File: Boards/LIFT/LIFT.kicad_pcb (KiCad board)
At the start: 4 copper layers, 58 x 82.5 mm, 11 parts, among them J1 Screw_Terminal_01x02, J2 393570004, J3 393570004, J4 393570004, J5 Screw_Terminal_01x02, U3 MAX485_MODULE_5V_LOGIC_TLL_TO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

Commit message: PCB Loadcells
Agora sim acho que ta acabado
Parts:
- added G***: LOGO, FEUP-text:Feup-text, B.Cu at (158.0, 144.5)
- added U6: ~, DCDCModule:DCDC_Module, F.Cu at (155.0, 137.9)
- U2: moved to B.Cu
- moved U2 22.2 mm to (134.4, 136.3), turned to 90 degrees
- moved J1 7.79 mm to (174.5, 138.8)
- moved A1 0.11 mm to (176.8, 88.7)
- moved U3 0.11 mm to (146.1, 116.2)
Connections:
- J1 pad 2: /3V3 -> /V_In
- J3 pad 3: /A1+ -> /A1-
- J3 pad 4: /A1- -> /A1+
- J4 pad 3: /A3+ -> /A3-
- J4 pad 4: /A3- -> /A3+
- U1 pad 3: /A3+ -> /A3-
- U1 pad 4: /A3- -> /A3+
- U4 pad 3: /A1+ -> /A1-
- U4 pad 4: /A1- -> /A1+
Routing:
- net /5V: track 92.6 -> 164.9 mm, vias 0 -> 1
- net GND: track 0.00 -> 51.3 mm
- net /SD_CLK: track 44.7 -> 61.2 mm
- net /SD_MOSI: track 43.2 -> 56.4 mm
- net /SD_CS: track 43.7 -> 56.8 mm
- net /V_In: track 0.00 -> 9.90 mm
- net /SD_MISO: track 59.8 -> 68.3 mm
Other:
- board size 58 x 82.5 mm -> 59 x 100 mm
- board text added: "Green White Black Red"
- board text added: "LIFT"
- board text added: "RS+ RS-"

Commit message: PCB LOADCELLS
PCB LOADCELLS
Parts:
- U2: moved to F.Cu
- moved U2 11.6 mm to (122.8, 136.4)
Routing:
- net GND: track 51.3 -> 34.1 mm
- net /SD_CS: track 56.8 -> 54.2 mm
- net /SD_MISO: track 68.3 -> 66.7 mm
- net /SD_MOSI: track 56.4 -> 54.9 mm
- net /SD_CLK: track 61.2 -> 59.8 mm

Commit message: PCB Lift Final
PCB Lift Final
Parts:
- moved G*** 3.01 mm to (155.0, 144.2)
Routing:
- net GND: track 34.1 -> 11.6 mm
- net /5V: track 164.9 -> 166.2 mm, vias 1 -> 0
- net /V_In: track 9.90 -> 11.1 mm
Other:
- board text added: "LEAVE SPACE FOR SD CARD"

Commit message: LIFT Finish
LIFT pcb finish
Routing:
- added copper zone on B.Cu, net /3V3
- added copper zone on F.Cu, net GND
- removed copper zone on In2.Cu, net /3V3
- removed copper zone on In1.Cu, net GND
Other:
- copper layers 4 -> 2

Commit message: LIFT PCB
LIFT PCB
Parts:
- added H1: MountingHole, MountingHole:MountingHole_3.2mm_M3, F.Cu at (185.8, 138.2)
- added H3: MountingHole, MountingHole:MountingHole_3.2mm_M3, F.Cu at (185.5, 58.2)
- added H4: MountingHole, MountingHole:MountingHole_3.2mm_M3, F.Cu at (117.5, 58.5)
- added H5: MountingHole, MountingHole:MountingHole_3.2mm_M3, F.Cu at (117.5, 138.2)
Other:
- board size 59 x 100 mm -> 75 x 100 mm

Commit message: PCB LIFT
PCB LIFT
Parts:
- added J6: Screw_Terminal_01x02, TerminalBlock_4Ucon:TerminalBlock_4Ucon_1x02_P3.50mm_Horizontal, F.Cu at (173.8, 127.0)
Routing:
- net /RS-: track 7.99 -> 21.3 mm
- net /RS+: track 7.99 -> 20.4 mm

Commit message: LIFT PCB
LIFT PCB FINAL
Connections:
- A1 pad 10: /SD_MOSI -> unconnected-(A1-GPIO7-Pad10)
- A1 pad 16: unconnected-(A1-GPIO12-Pad16) -> /UART TX
- A1 pad 17: unconnected-(A1-GPIO13-Pad17) -> /UART RX
- A1 pad 21: /UART TX -> /SD_MISO
- A1 pad 22: /UART RX -> /SD_CS
- A1 pad 24: unconnected-(A1-GPIO18-Pad24) -> /SD_CLK
- A1 pad 25: unconnected-(A1-GPIO19-Pad25) -> /SD_MOSI
- A1 pad 6: /SD_MISO -> unconnected-(A1-GPIO4-Pad6)
- A1 pad 7: /SD_CS -> unconnected-(A1-GPIO5-Pad7)
- A1 pad 9: /SD_CLK -> unconnected-(A1-GPIO6-Pad9)
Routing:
- net /3V3: track 0.00 -> 89.4 mm
- net /SD_MISO: track 66.7 -> 36.0 mm
- net /SD_CS: track 54.2 -> 25.4 mm
- net /SD_CLK: track 59.8 -> 34.4 mm
- net /SD_MOSI: track 54.9 -> 30.8 mm
- net /UART TX: track 16.8 -> 37.2 mm
- net /UART RX: track 8.24 -> 28.2 mm
- added copper zone on B.Cu, net GND
- removed copper zone on B.Cu, net /3V3

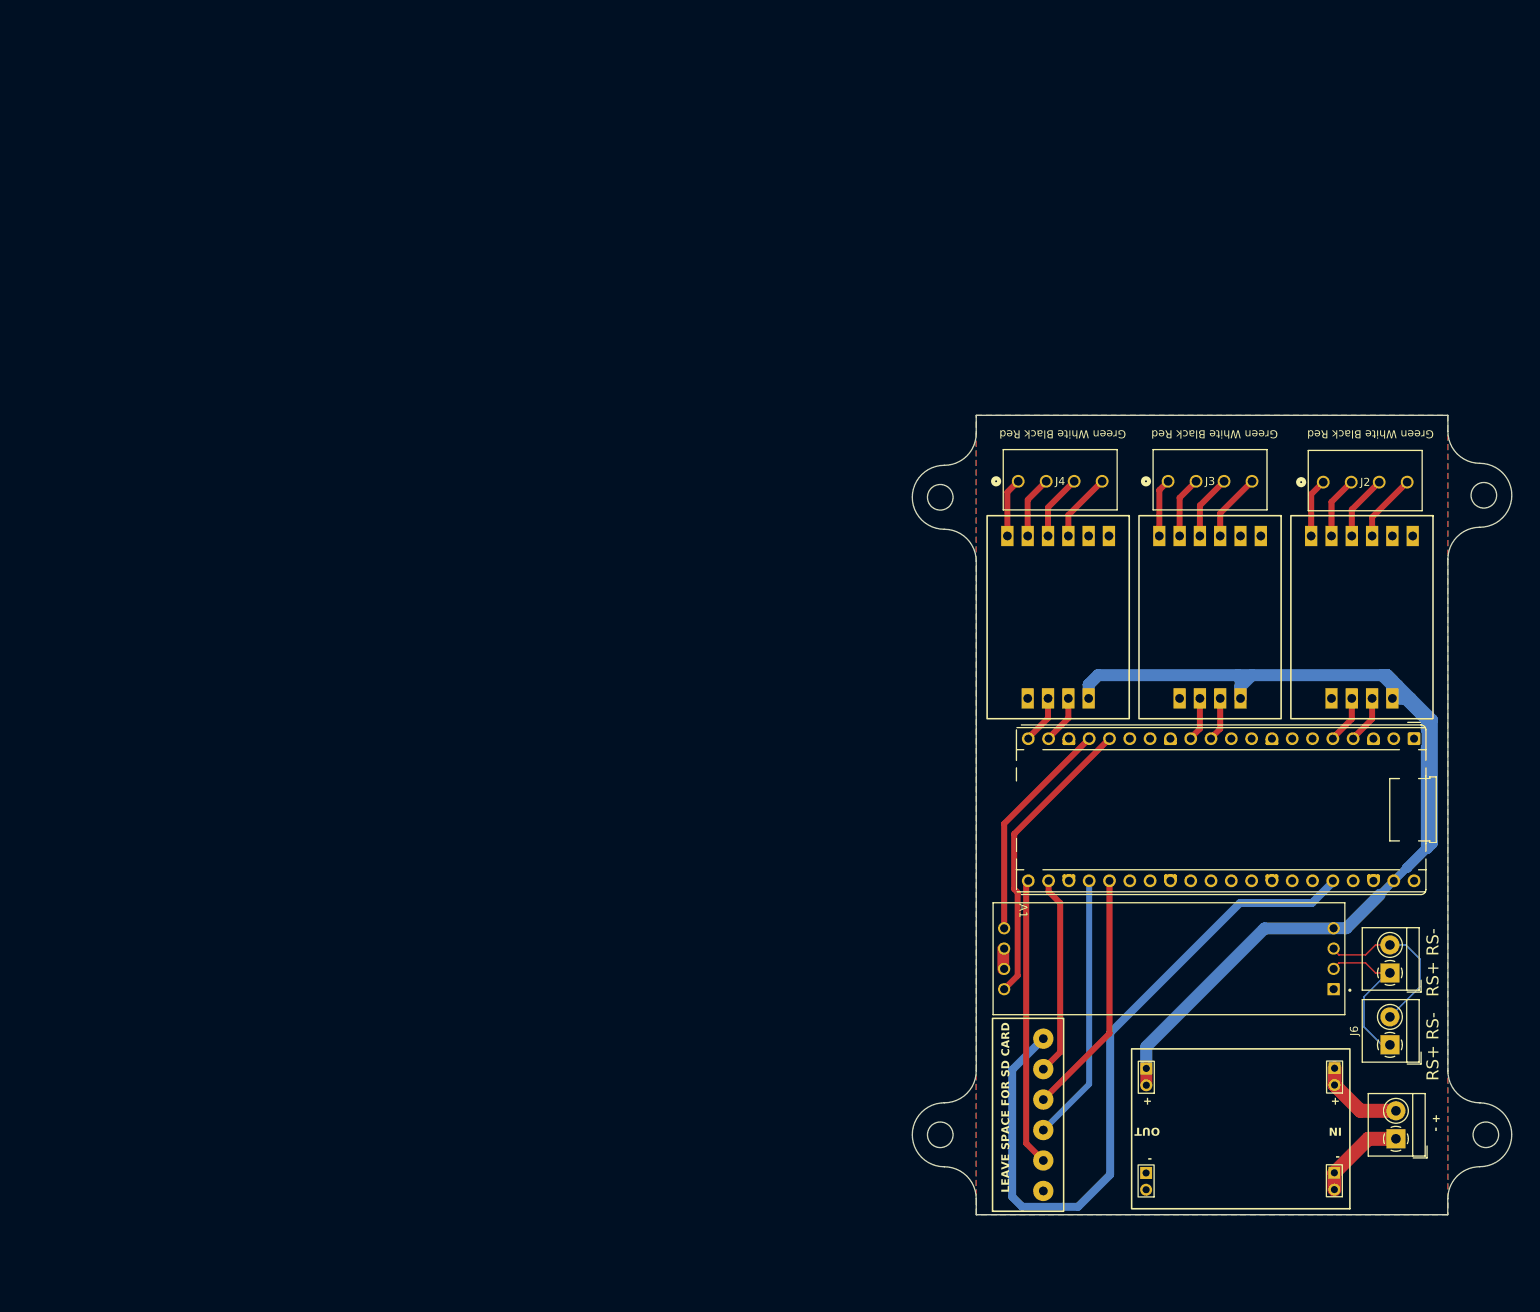
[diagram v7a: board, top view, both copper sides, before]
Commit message: PCB LIFT CAN BUS
adicionei um controlador de can para futuras implementaçoes
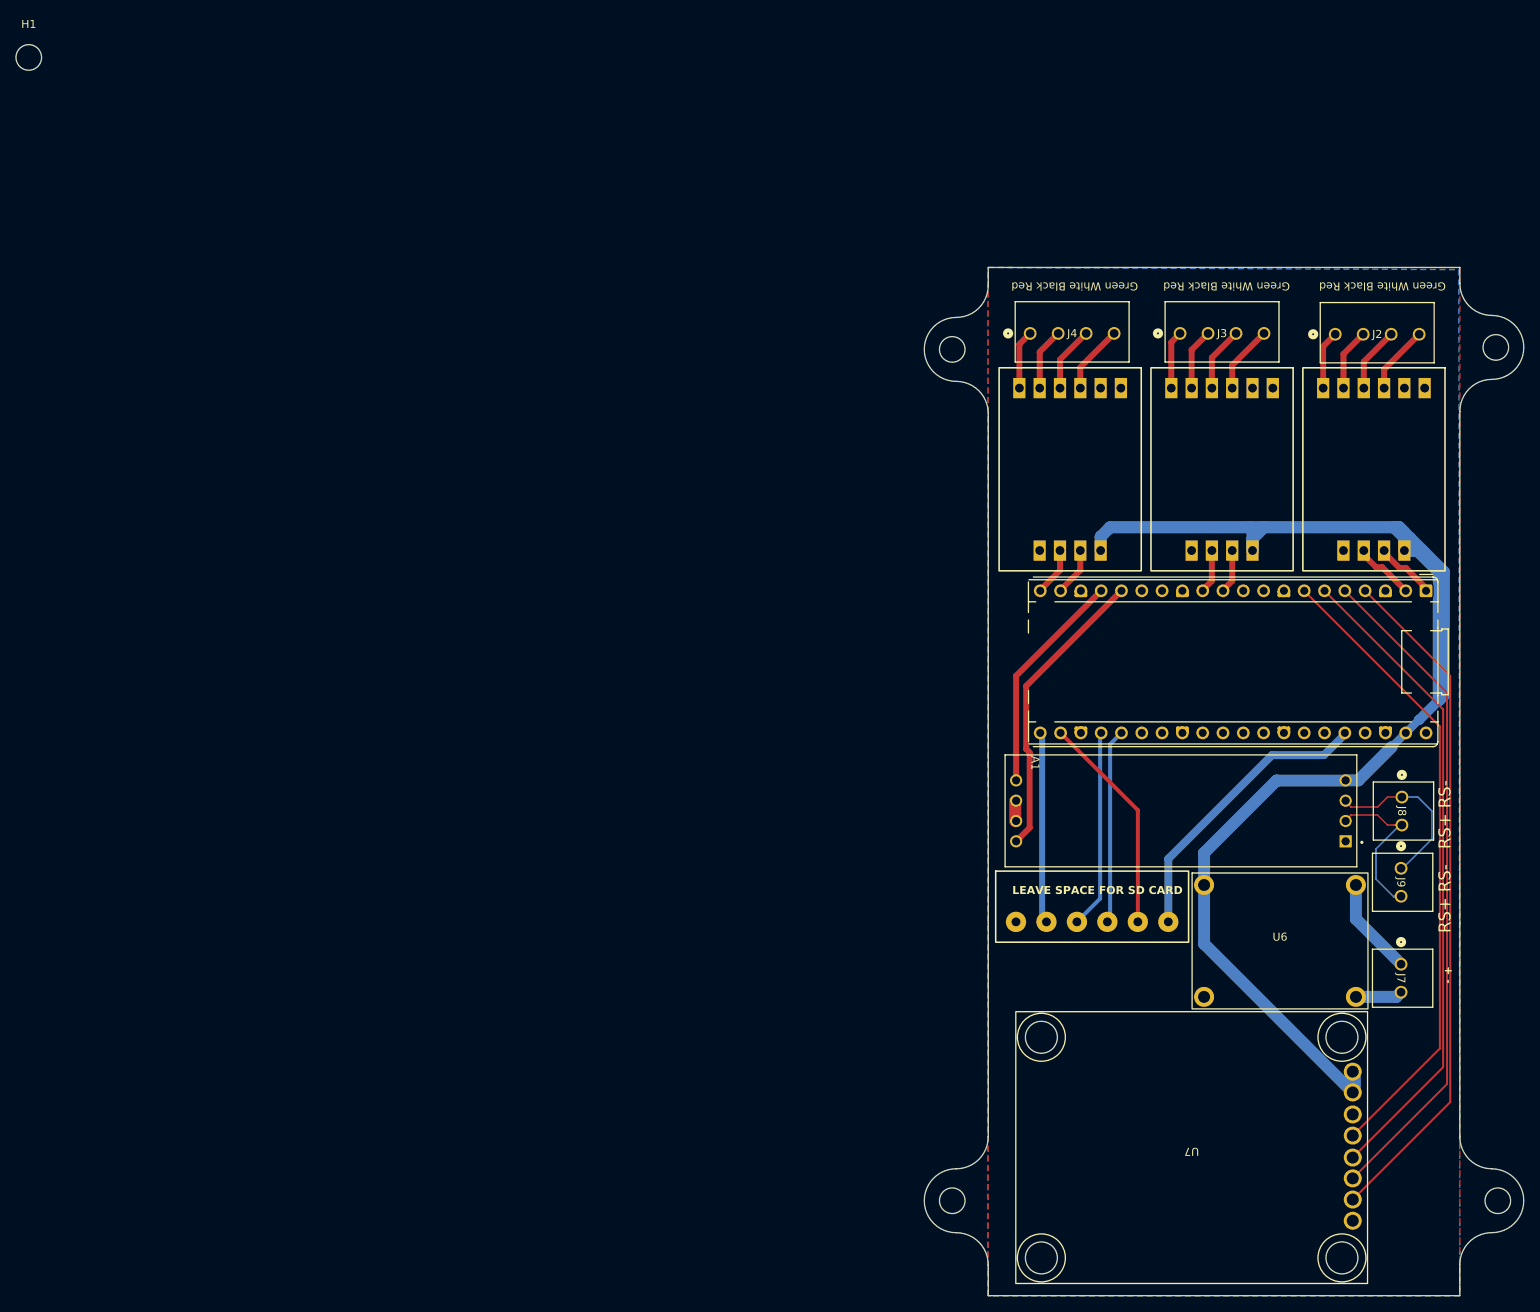
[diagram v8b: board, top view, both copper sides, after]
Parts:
- removed the H1 at (185.8, 138.2)
- removed J1, J5, J6: Screw_Terminal_01x02, TerminalBlock_4Ucon:TerminalBlock_4Ucon_1x02_P3.50mm_Horizontal
- added H1: MountingHole, MountingHole:MountingHole_3.2mm_M3, F.Cu at (187.2, 146.5)
- added H1: MountingHole, MountingHole:MountingHole_3.2mm_M3, F.Cu at (3.48, 3.48)
- added J7: 393570002, CONN_SD-39357-001_02P_MOL:CONN_SD-39357-001_02P_MOL, F.Cu at (175.1, 116.9)
- added J8: 393570002, CONN_SD-39357-001_02P_MOL:CONN_SD-39357-001_02P_MOL, F.Cu at (175.2, 96.0)
- added J9: 393570002, CONN_SD-39357-001_02P_MOL:CONN_SD-39357-001_02P_MOL, F.Cu at (175.1, 104.9)
- added U7: ~, CANController:CANController, F.Cu at (148.9, 139.8)
- U6: footprint DCDCModule:DCDC_Module -> minidcdc:MiniDCDC
- moved U2 34.9 mm to (135.9, 104.0), turned to 0 degrees
- moved U6 24.4 mm to (160.0, 114.0), turned to 0 degrees
- moved A1 18.6 mm to (178.3, 70.2)
- moved H3 18.6 mm to (187.0, 39.8)
- moved H4 18.6 mm to (119.0, 40.0)
- moved J2 18.6 mm to (166.9, 38.1)
- moved J3 18.6 mm to (147.5, 38.0)
- moved J4 18.6 mm to (128.7, 38.0)
- moved U1 18.6 mm to (135.0, 55.0)
- moved U3 18.6 mm to (147.6, 97.7)
- moved U4 18.6 mm to (154.0, 55.0)
- moved U5 18.6 mm to (173.0, 55.0)
- moved G*** 14.4 mm to (145.6, 155.2)
- moved H5 8.39 mm to (119.0, 146.5)
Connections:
- A1 pad 1: unconnected-(A1-GPIO0-Pad1) -> /CLK3
- A1 pad 2: unconnected-(A1-GPIO1-Pad2) -> /DT3
- A1 pad 4: /CLK3 -> /CAN CLK
- A1 pad 5: /DT3 -> /CAN TX
- A1 pad 6: unconnected-(A1-GPIO4-Pad6) -> /CAN RX
- A1 pad 7: unconnected-(A1-GPIO5-Pad7) -> /CAN CS
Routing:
- net /CAN CLK: track 0.00 -> 85.6 mm
- net /CAN TX: track 0.00 -> 83.7 mm
- net /CAN RX: track 0.00 -> 81.7 mm
- net /CAN CS: track 0.00 -> 79.7 mm
- net /3V3: track 89.4 -> 36.6 mm
- net /5V: track 166.2 -> 193.5 mm
- net /SD_MISO: track 36.0 -> 24.3 mm
- net /SD_CLK: track 34.4 -> 24.9 mm
- net /SD_MOSI: track 30.8 -> 24.4 mm
- net GND: track 11.6 -> 5.89 mm
- net /SD_CS: track 25.4 -> 28.0 mm
- net /RS+: track 20.4 -> 22.6 mm
- net /DT3: track 6.09 -> 7.74 mm
- net /CLK3: track 6.09 -> 7.68 mm
- net /V_In: track 11.1 -> 12.2 mm
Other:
- board size 75 x 100 mm -> 75 x 128.6 mm
